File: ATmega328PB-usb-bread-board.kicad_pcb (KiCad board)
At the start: 2 copper layers, 60 x 60 mm, 31 parts, among them J1 Conn_01x17, J2 Conn_01x17, J3 USB_B_Micro, J4 AVR-ISP-6, J5 Grove-I2C-connector, J6 Grove-I2C-connector, J7 Grove-I2C-connector, U1 ATmega328PB-MU, U2 CP2102N-A01-GQFN28, U5 SiT2001B-MEMS-Clock-Generator

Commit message: Add USB pads
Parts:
- added J8: USB_test, my-kicad-footprints:2x02_P2.54mm_USB_Pads, B.Cu at (137.1, 94.8)
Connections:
- net Net-(D1-Pad2) renamed /D+
- net Net-(D1-Pad3) renamed /D-
- net Net-(D1-Pad6) renamed VBUS
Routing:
- net /D-: track 13.9 -> 26.0 mm, vias 1 -> 3
- net /D+: track 14.8 -> 23.5 mm, vias 1 -> 2
- net VBUS: track 30.9 -> 39.6 mm, vias 2 -> 3
- net GND: track 231.4 -> 229.3 mm, vias 39 -> 38

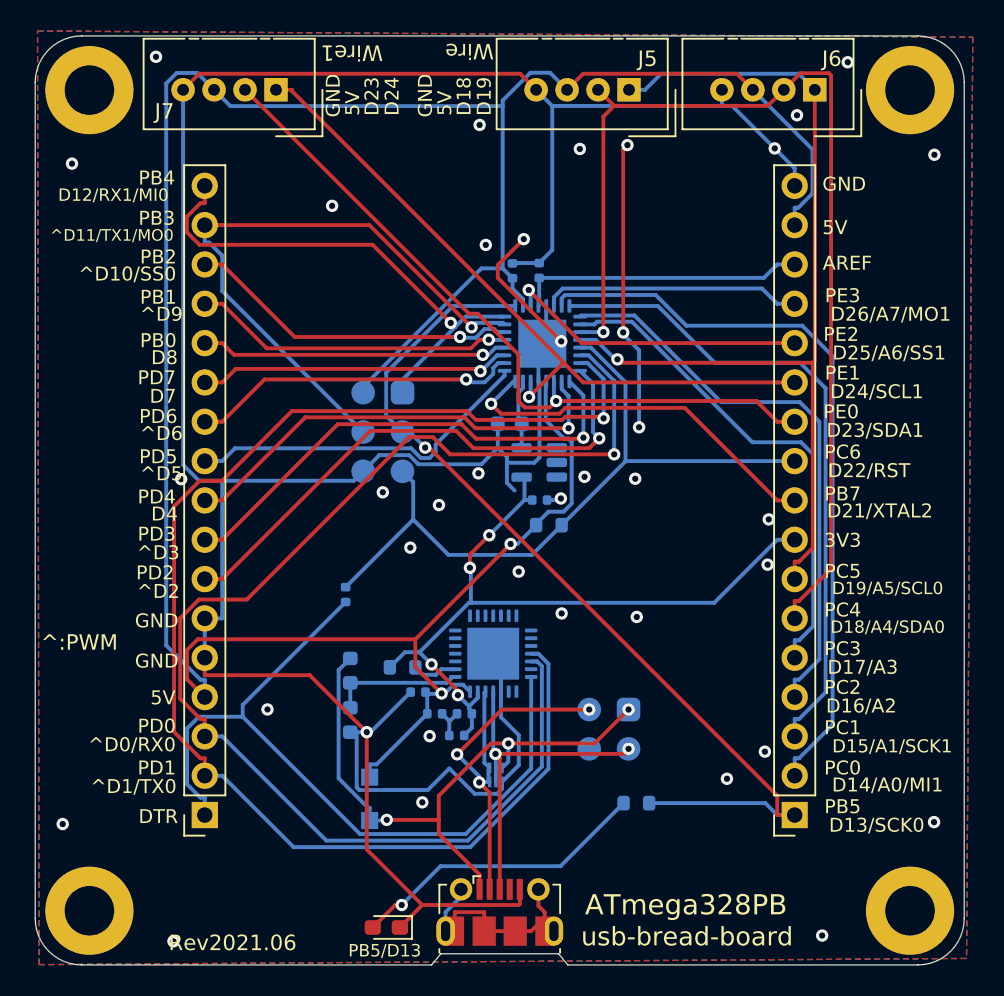
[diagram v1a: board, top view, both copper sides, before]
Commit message: Add reset button
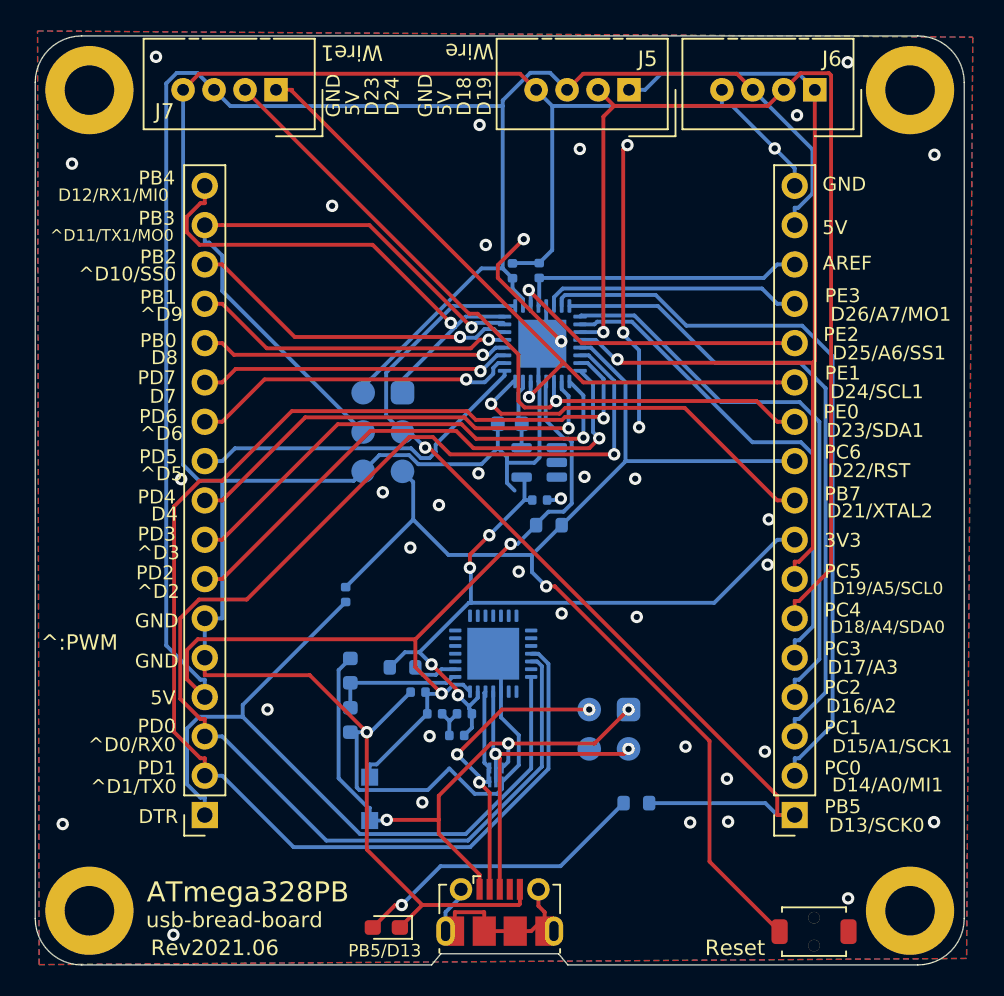
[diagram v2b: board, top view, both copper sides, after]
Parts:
- added SW1: SW_Push, my-kicad-footprints:SW_Push_TVAF06, F.Cu at (150.3, 107.8)
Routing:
- net /pc6: track 46.6 -> 77.9 mm, vias 0 -> 1
- net GND: vias 38 -> 41
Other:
- board text added: "Reset"

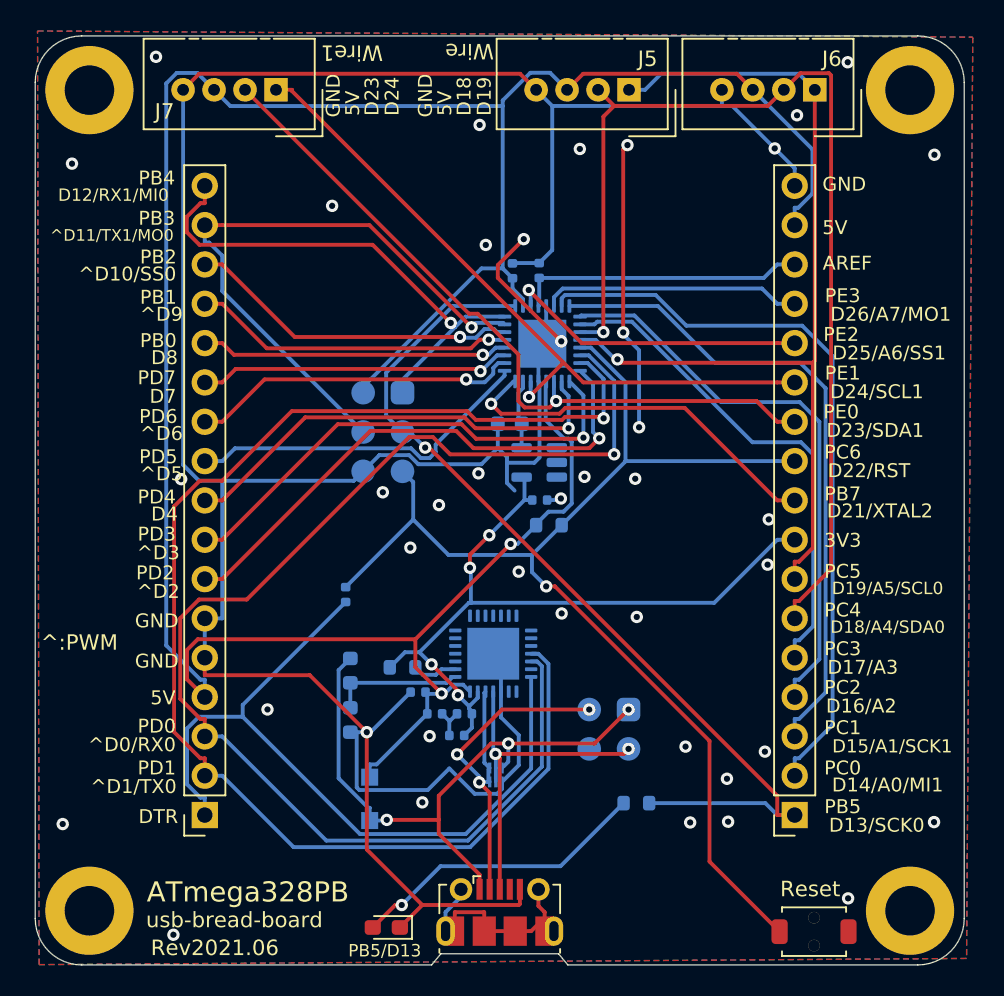
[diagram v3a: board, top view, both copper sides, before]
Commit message: Change position of D13
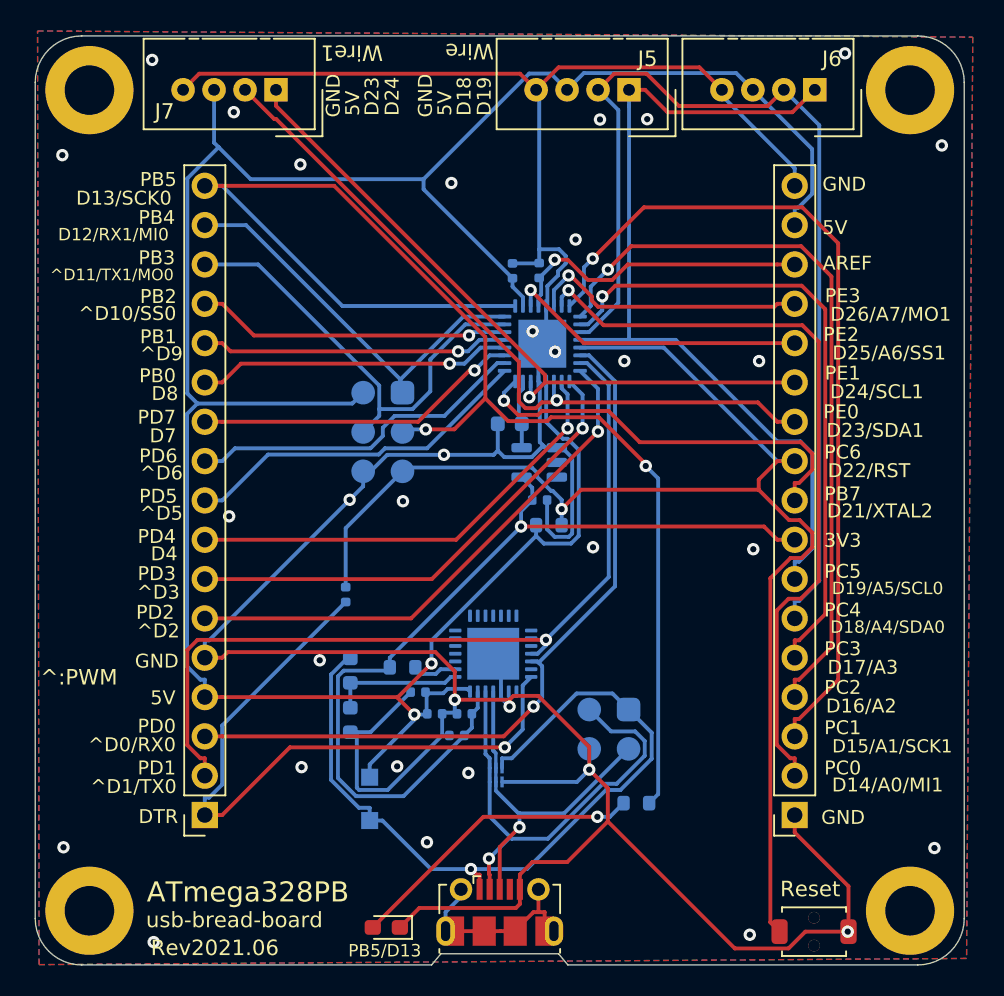
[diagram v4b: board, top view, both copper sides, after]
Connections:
- J1 pad 10: /pd5 -> /pd6
- J1 pad 11: /pd6 -> /pd7
- J1 pad 12: /pd7 -> /pb0
- J1 pad 13: /pb0 -> /pb1
- J1 pad 14: /pb1 -> /pb2
- J1 pad 15: /pb2 -> /pb3
- J1 pad 16: /pb3 -> /pb4
- J1 pad 17: /pb4 -> /pb5
- J1 pad 6: GND -> /pd2
- J1 pad 7: /pd2 -> /pd3
- J1 pad 8: /pd3 -> /pd4
- J1 pad 9: /pd4 -> /pd5
- J2 pad 1: /pb5 -> GND
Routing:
- net /USB_UART_TX: track 83.3 -> 48.9 mm
- net /USB_UART_RX: track 87.9 -> 54.3 mm
- net /pb5: track 60.4 -> 90.4 mm, vias 1 -> 2
- net /pc1: track 42.2 -> 55.1 mm, vias 0 -> 1
- net VBUS: track 39.6 -> 51.4 mm, vias 3 -> 1
- net /pc2: track 36.9 -> 48.0 mm, vias 0 -> 1
- net /pb3: track 40.0 -> 29.5 mm, vias 1 -> 0
- net +3V3: track 47.9 -> 58.0 mm, vias 4 -> 1
- net /pc6: track 77.9 -> 87.8 mm
- net /pc3: track 32.5 -> 41.5 mm, vias 0 -> 1
- net VCC: track 175.1 -> 167.2 mm
- net /pb4: track 32.6 -> 26.1 mm, vias 1 -> 0
- net /DTR: track 49.7 -> 44.1 mm, vias 0 -> 1
- net /pc5: track 60.8 -> 56.1 mm, vias 1 -> 0
- net /D-: track 26.0 -> 30.3 mm, vias 3 -> 1
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
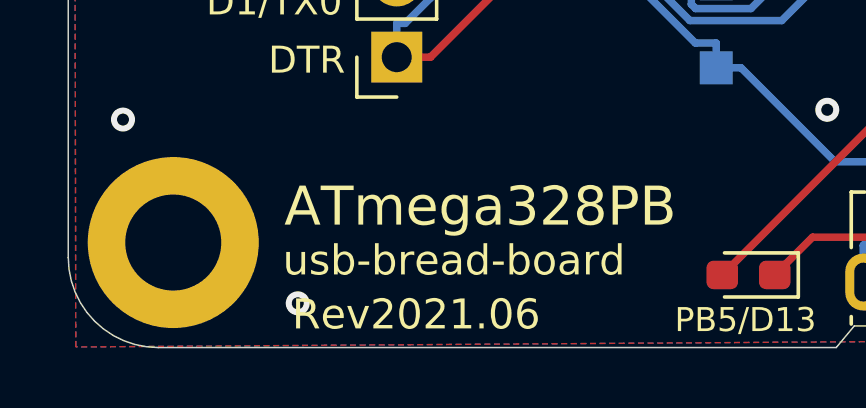
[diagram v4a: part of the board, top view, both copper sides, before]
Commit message: Update to Rev2021.07
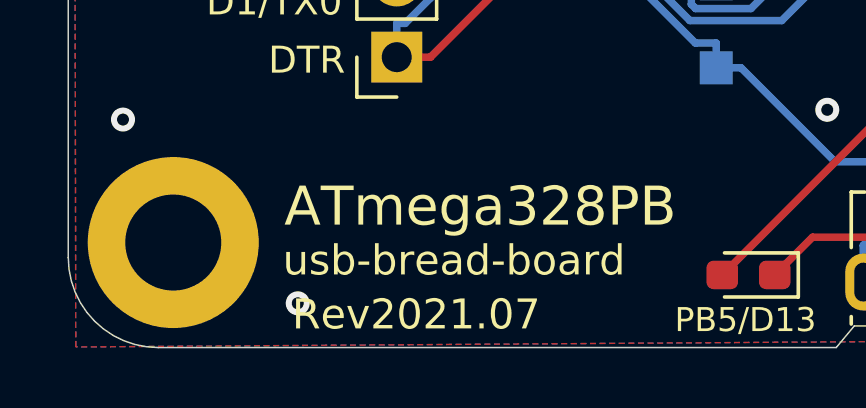
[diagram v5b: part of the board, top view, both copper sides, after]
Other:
- board text added: "Rev2021.07"
- board text removed: "Rev2021.06"
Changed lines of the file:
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@@
     (effects (font (size 1 1) (thickness 0.15)))
   )
-  (gr_text Rev2021.06 (at 111.6 108.9) (layer F.SilkS)
+  (gr_text Rev2021.07 (at 111.6 108.9) (layer F.SilkS)
     (effects (font (size 1 1) (thickness 0.2)))
   )
